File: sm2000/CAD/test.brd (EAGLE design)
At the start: 160 x 100 mm, 30 parts, among them Q1 BRF92, Q2 BFQ19, Q3 BFQ19, X1 BU-SMA-G, X2 BU-SMA-G

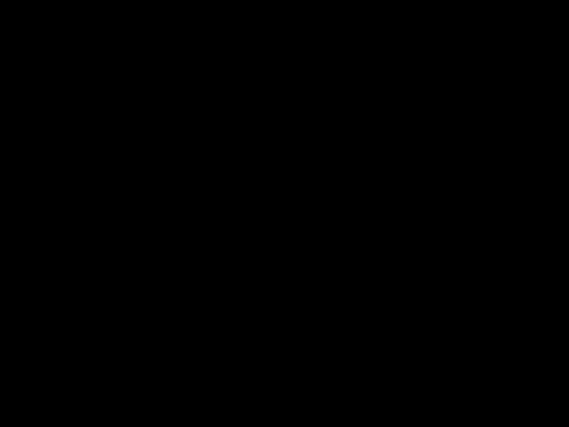
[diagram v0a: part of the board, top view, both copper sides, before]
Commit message: 
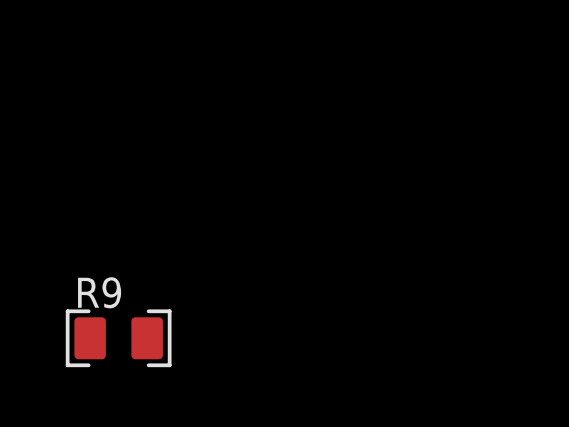
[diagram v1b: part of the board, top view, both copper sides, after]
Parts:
- added R9: 10k, AA-ipc-7351-resistor:RESC2012X70N
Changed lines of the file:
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@@
 <element name="C9" library="rcl" package="C025-024X044" value="22p" x="-53.22" y="86.25"/>
 <element name="C10" library="_RoweTel" package="TRIMCAP_VAR_2222_V" value="TRIMCAP_VAR_2222_V" x="-19" y="47"/>
+<element name="R9" library="AA-ipc-7351-resistor" package="RESC2012X70N" value="10k" x="-53.5" y="-2.5"/>
 </elements>
 <signals>

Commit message: test - removed resistor from schematic
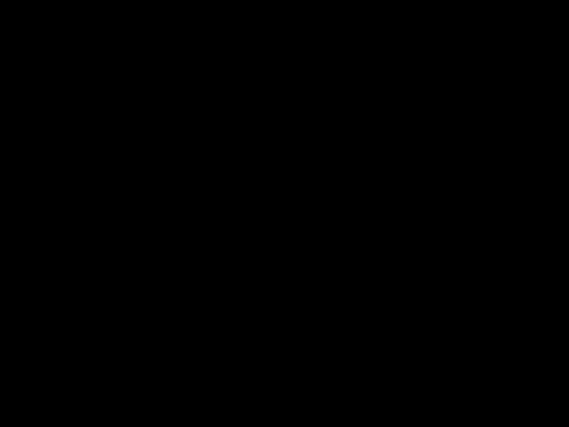
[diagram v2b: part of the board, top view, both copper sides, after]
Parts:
- removed R9: 10k, AA-ipc-7351-resistor:RESC2012X70N
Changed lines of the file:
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@@
 <element name="C9" library="rcl" package="C025-024X044" value="22p" x="-53.22" y="86.25"/>
 <element name="C10" library="_RoweTel" package="TRIMCAP_VAR_2222_V" value="TRIMCAP_VAR_2222_V" x="-19" y="47"/>
-<element name="R9" library="AA-ipc-7351-resistor" package="RESC2012X70N" value="10k" x="-53.5" y="-2.5"/>
 </elements>
 <signals>
